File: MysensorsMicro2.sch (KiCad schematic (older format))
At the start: 29 parts, among them P1 Debug, P2 MYSX_1.2, P3 Antenna, U1 ATSAMD21E, U2 AP1117D33, U3 NRF24L01, U4 RFM69HW, U5 ATSHA204A, U6 AT25DF512C, U7 Si7021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

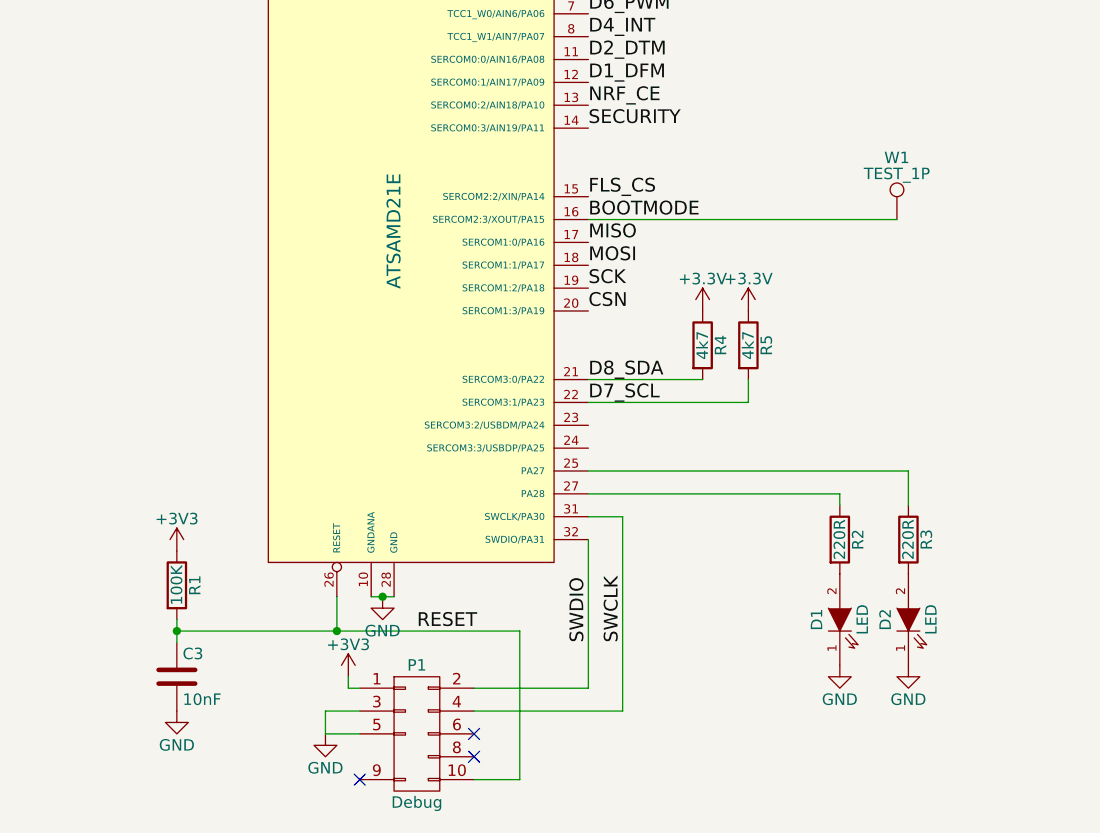
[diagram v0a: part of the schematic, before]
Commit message: Added testpads to reset signal + gnd
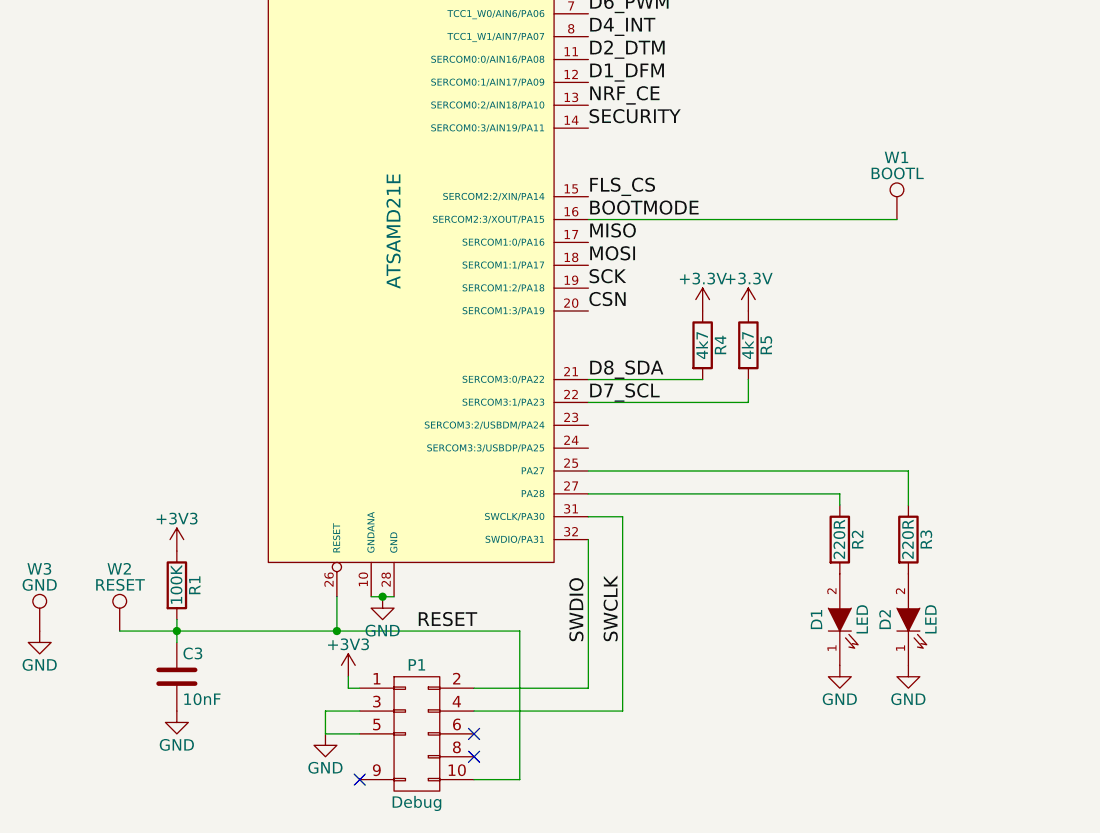
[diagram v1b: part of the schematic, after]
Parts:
- added W2: RESET, Measurement_Points:Measurement_Point_Round-SMD-Pad_Small, symbol TEST_1P
- added W3: GND, Measurement_Points:Measurement_Point_Round-SMD-Pad_Small, symbol TEST_1P
- W1: value TEST_1P -> BOOTL
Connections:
- net GND: now also W3.1
- net RESET: now also W2.1
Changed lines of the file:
@@
 	3300 7300 3300 6650
 Wire Wire Line
-	3300 6650 1800 6650
+	3300 6650 1550 6650
 Wire Wire Line
 	2500 6650 2500 6500
@@
 P 4950 4850
 F 0 "W1" H 4950 5120 50  0000 C CNN
-F 1 "TEST_1P" H 4950 5050 50  0000 C CNN
+F 1 "BOOTL" H 4950 5050 50  0000 C CNN
 F 2 "Measurement_Points:Measurement_Point_Round-SMD-Pad_Small" H 5150 4850 50  0001 C CNN
 F 3 "" H 5150 4850 50  0000 C CNN
@@
 07 00 85 88 3B 00 28 44 DC 01 40 21 E2 0E 00 0A 11 77 00 50 88 B8 03 80 42 C4 1D 00 14 22 EE 00
 A0 10 71 07 00 85 88 3B 00 28 F4 2F 6E 0E 73 66 69 F5 31 42 00 00 00 00 49 45 4E 44 AE 42 60 82
-00
+58
 EndData
 $EndBitmap
+$Comp
+L TEST_1P W2
+U 1 1 56BE268C
+P 1550 6650
+F 0 "W2" H 1550 6920 50  0000 C CNN
+F 1 "RESET" H 1550 6850 50  0000 C CNN
+F 2 "Measurement_Points:Measurement_Point_Round-SMD-Pad_Small" H 1750 6650 50  0001 C CNN
+F 3 "" H 1750 6650 50  0000 C CNN
+	1    1550 6650
+	1    0    0    -1
+$EndComp
+$Comp
+L GND #PWR036
+U 1 1 56BE2C3B
+P 1200 6650
+F 0 "#PWR036" H 1200 6400 50  0001 C CNN
+F 1 "GND" H 1200 6500 50  0000 C CNN
+F 2 "" H 1200 6650 50  0000 C CNN
+F 3 "" H 1200 6650 50  0000 C CNN
+	1    1200 6650
+	1    0    0    -1
+$EndComp
+$Comp
+L TEST_1P W3
+U 1 1 56BE2E1D
+P 1200 6650
+F 0 "W3" H 1200 6920 50  0000 C CNN
+F 1 "GND" H 1200 6850 50  0000 C CNN
+F 2 "Measurement_Points:Measurement_Point_Round-SMD-Pad_Small" H 1400 6650 50  0001 C CNN
+F 3 "" H 1400 6650 50  0000 C CNN
+	1    1200 6650
+	1    0    0    -1
+$EndComp
 $EndSCHEMATC
